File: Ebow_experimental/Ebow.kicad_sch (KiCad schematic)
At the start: 10 parts, among them J1 Conn_01x02, U1 LM386

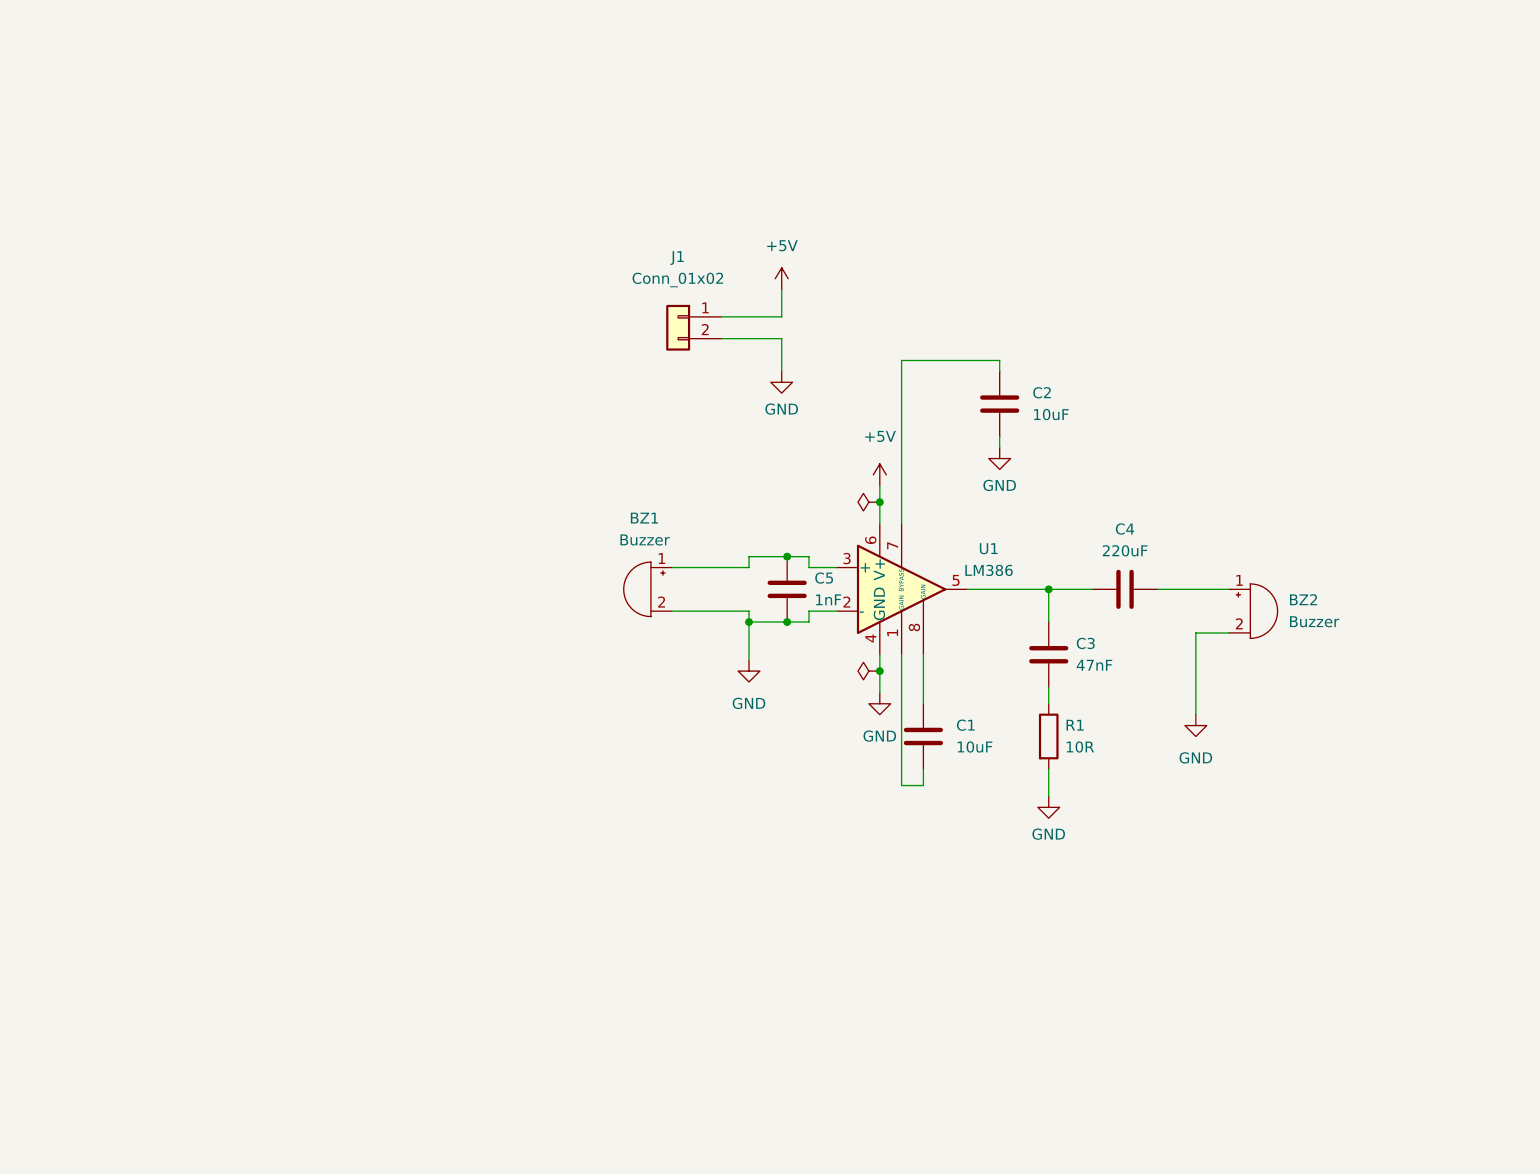
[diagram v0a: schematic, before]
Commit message: spread schema design out on page and generated pdf
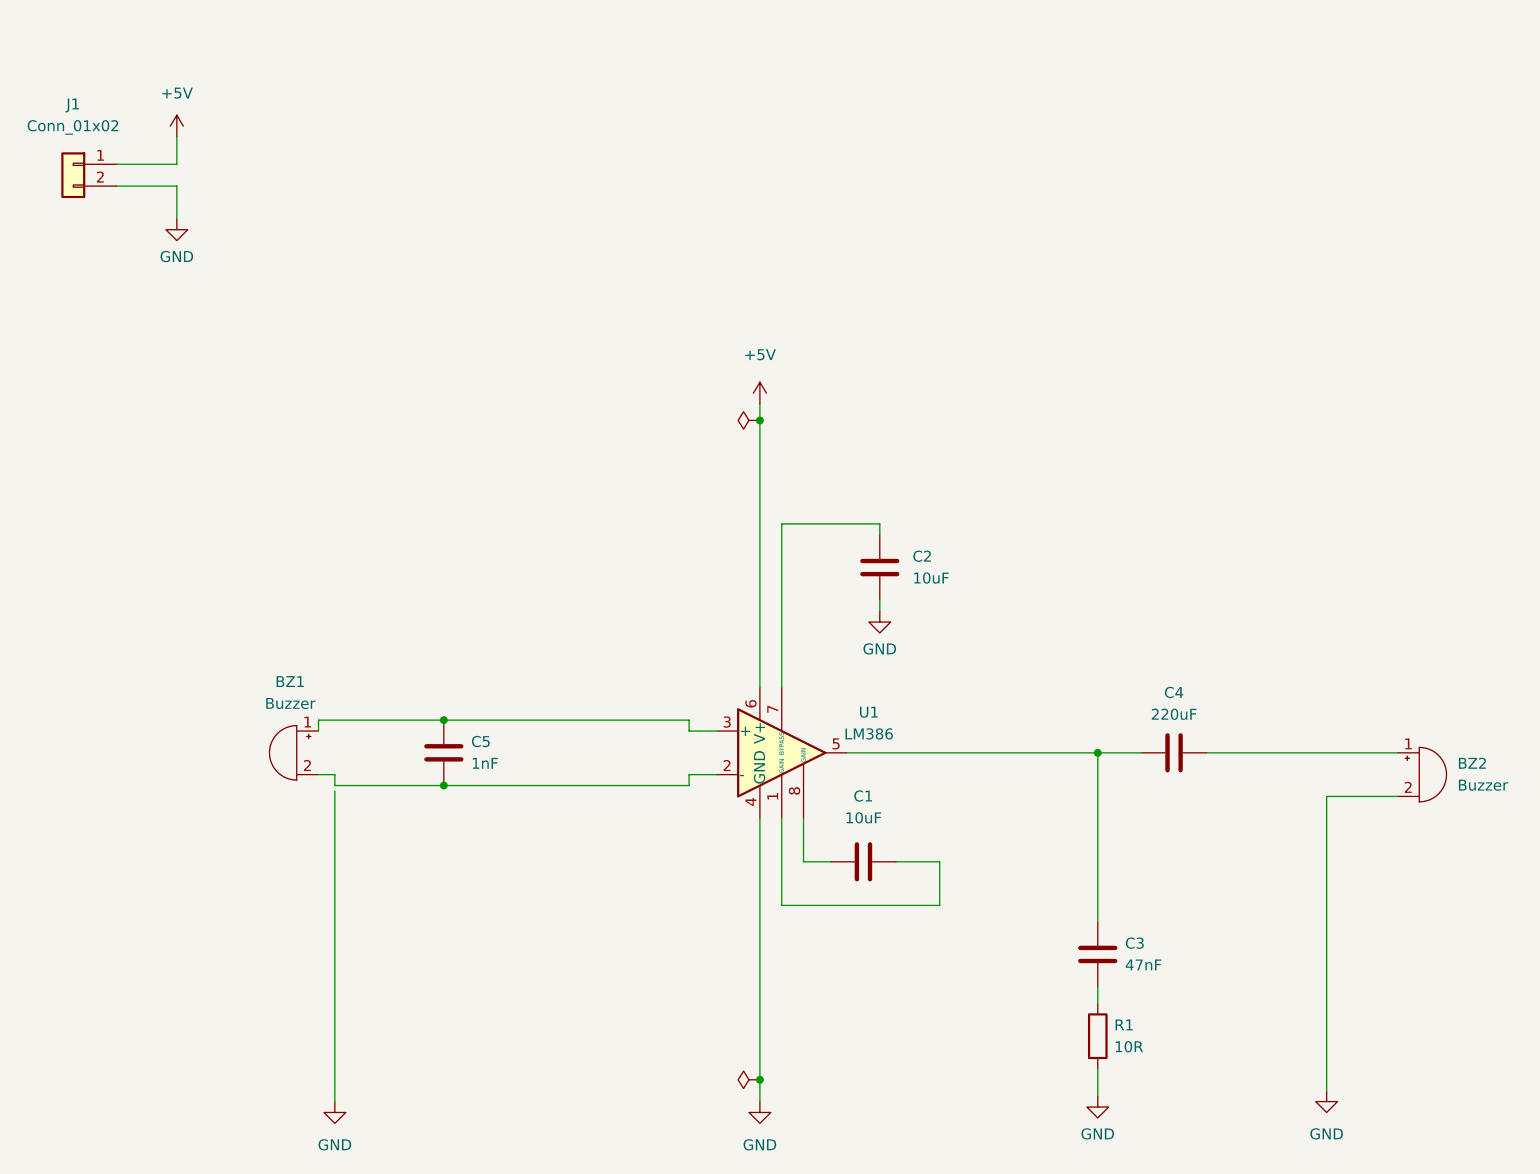
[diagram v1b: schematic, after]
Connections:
- net GND: no longer BZ1.2 (+), C5.1, U1.2 (-)
- new net: BZ1.2 (+), C5.1, U1.2 (-)
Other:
- moved on the sheet: BZ1, BZ2, C1, C2, C3, C4, C5, J1, R1, U1

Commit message: Reconfigured as THT
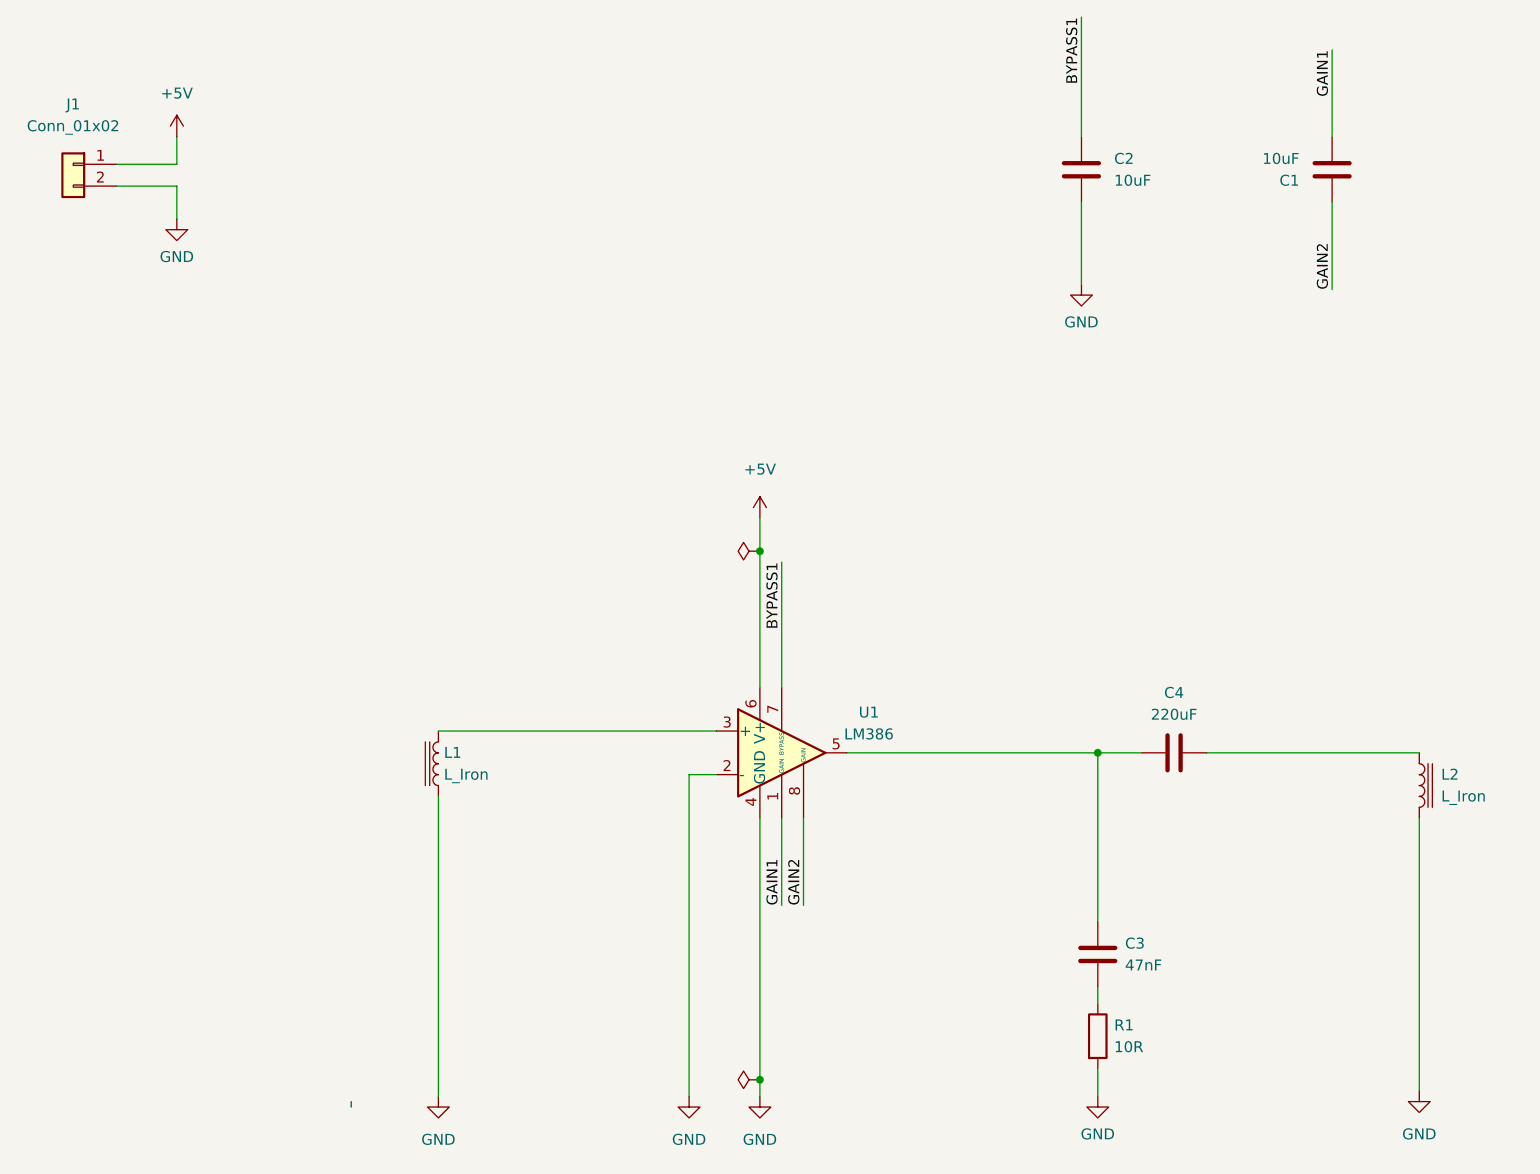
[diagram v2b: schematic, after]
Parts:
- removed BZ1, BZ2: Buzzer, Buzzer_Beeper:MagneticBuzzer_Kingstate_KCG0601, symbol Device:Buzzer
- removed C5: 1nF, Capacitor_SMD:C_1206_3216Metric_Pad1.33x1.80mm_HandSolder, symbol Device:C
- added L1, L2: L_Iron, Buzzer_Beeper:Buzzer_D14mm_H7mm_P10mm, symbol Device:L_Iron
- C1, C2: footprint Capacitor_SMD:C_1206_3216Metric_Pad1.33x1.80mm_HandSolder -> Capacitor_THT:CP_Radial_D5.0mm_P2.00mm
- C3: footprint Capacitor_SMD:C_1206_3216Metric_Pad1.33x1.80mm_HandSolder -> Capacitor_THT:C_Disc_D3.0mm_W2.0mm_P2.50mm
- C4: footprint Capacitor_SMD:C_Elec_10x10.2 -> Capacitor_THT:CP_Radial_D8.0mm_P3.50mm
- R1: footprint Resistor_SMD:R_1206_3216Metric_Pad1.30x1.75mm_HandSolder -> Resistor_THT:R_Axial_DIN0207_L6.3mm_D2.5mm_P15.24mm_Horizontal
- U1: footprint Package_DIP:DIP-8_W7.62mm_SMDSocket_SmallPads -> Package_DIP:DIP-8_W7.62mm_Socket
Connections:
- net GND: now also U1.2 (-), L1.1, L2.2
- net BYPASS1: now reaches C2.1, U1.7 (BYPASS)
- net GAIN2: now reaches C1.1, U1.8 (GAIN)
- net GAIN1: now reaches C1.2, U1.1 (GAIN)
- net at U1.3 (+): now also L1.2
- net at C4.2: now also L2.1
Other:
- moved on the sheet: C2
